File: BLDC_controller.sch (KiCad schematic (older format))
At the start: 97 parts, among them P1 CONN_01X02, P2 CONN_01X06, P3 CONN_01X05, P4 CONN_01X03, P5 CONN_01X05, Q1 PSMN2R0-30YLD, Q2 PSMN2R0-30YLD, Q3 PSMN2R0-30YLD, Q4 PSMN2R0-30YLD, Q5 PSMN2R0-30YLD, Q6 PSMN2R0-30YLD

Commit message: mostly routed
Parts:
- removed C20, C25, C26, C27: 220n, project_footprints:C_0805, symbol C
- C10, C11, C16, C22, C23, C24, C8, C9: footprint project_footprints:C_0402 -> project_footprints:C_0603
- C15, C21: value C -> 10p
- R1, R2, R3, R30, R31, R32, R33, R34, R35, R4, R40, R5, R6: footprint project_footprints:R_0603_NOM -> project_footprints:R_0603
- R10, R11, R12, R13, R14, R15, R16, R17, R18, R19, R20, R21, R22, R23, R24, R25, R26, R27, R28, R29, R36, R38, R39, R41, R42, R43, R44, R45, R46, R47: footprint project_footprints:R_0402_MOST -> project_footprints:R_0603
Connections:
- net GND: now also R14.1, R15.1, R16.1; no longer R14.2, R15.2, R16.2
- net OP4P: now reaches D1.1 (OP4P), R29.1
- net OP4N: now reaches D1.2 (OP4N), R47.2
- net OP1P: now reaches D1.23 (OP1P), R17.1, R20.2, R23.1
- net VBOOSTW: now reaches C3.2, D1.27 (VBOOTW)
- net VBOOSTV: now reaches C2.2, D1.31 (VBOOTV)
- net VBOOSTU: now reaches C1.2, D1.35 (VBOOTU)
- net OP2P: now reaches D1.41 (OP2P), R18.1, R21.2, R24.1
- net OP3P: now reaches D1.45 (OP3P), R19.1, R22.2, R25.1
- net U_SENSE_N renamed OP3N
- net OP3N: now also R15.2; no longer R15.1
- net V_SENSE_N renamed OP2N
- net OP2N: now also R16.2; no longer R16.1
- net W_SENSE_N renamed OP1N
- net OP1N: now also R14.2; no longer R14.1
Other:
- moved on the sheet: C1, C2, C3, R14, R15, R16

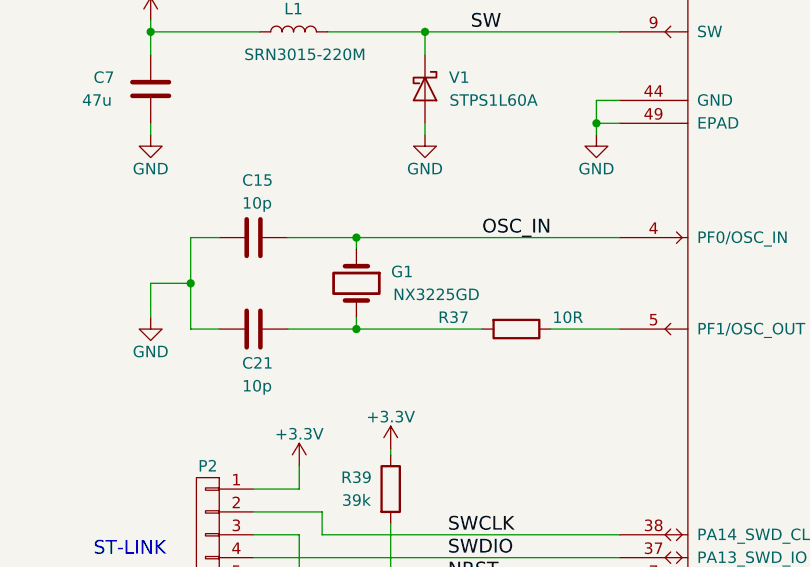
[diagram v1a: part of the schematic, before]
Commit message: keepouts added under sense resistors
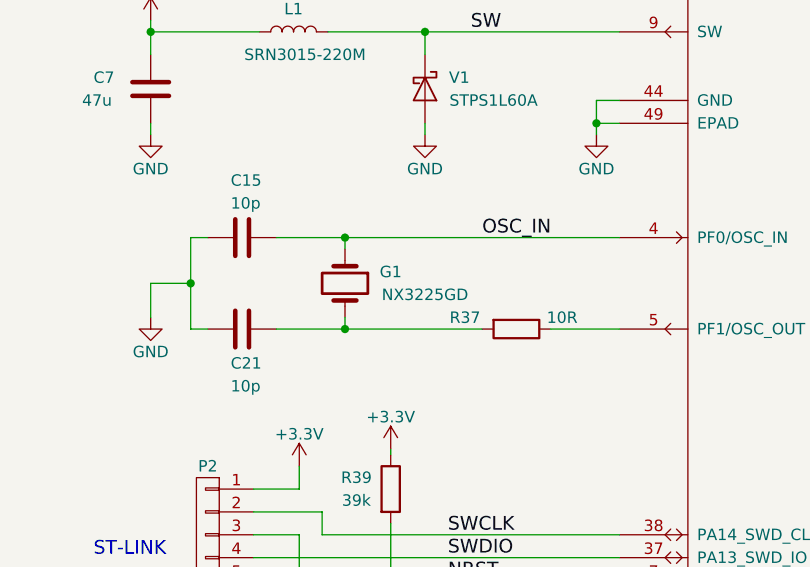
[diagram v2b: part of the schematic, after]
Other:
- moved on the sheet: C15, C21, G1
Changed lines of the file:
@@
 	6600 7900 7400 7900
-$Comp
-L R R37
-U 1 1 58A95F2B
-P 6950 3500
-F 0 "R37" V 6900 3225 50  0000 C CNN
-F 1 "10R" V 6900 3725 50  0000 C CNN
-F 2 "project_footprints:R_0402_MOST" V 6880 3500 50  0001 C CNN
-F 3 "" H 6950 3500 50  0000 C CNN
-	1    6950 3500
-	0    1    1    0
-$EndComp
 $Comp
 L GND #PWR051
@@
 $EndComp
 Wire Wire Line
-	6250 3150 6250 3100
-Wire Wire Line
-	5950 3100 7400 3100
-Wire Wire Line
-	6250 3450 6250 3500
+	6200 3150 6200 3100
+Wire Wire Line
+	5900 3100 7400 3100
+Wire Wire Line
+	6200 3450 6200 3500
 $Comp
 L C C15
 U 1 1 58AA5F93
-P 5800 3100
-F 0 "C15" V 5550 3050 50  0000 L CNN
-F 1 "10p" V 5650 3050 50  0000 L CNN
-F 2 "project_footprints:C_0402" H 5838 2950 50  0001 C CNN
-F 3 "" H 5800 3100 50  0000 C CNN
-	1    5800 3100
+P 5750 3100
+F 0 "C15" V 5500 3050 50  0000 L CNN
+F 1 "10p" V 5600 3050 50  0000 L CNN
+F 2 "project_footprints:C_0402" H 5788 2950 50  0001 C CNN
+F 3 "" H 5750 3100 50  0000 C CNN
+	1    5750 3100
 	0    1    1    0
 $EndComp
-Wire Wire Line
-	7100 3500 7400 3500
-Wire Wire Line
-	5950 3500 6800 3500
 $Comp
 L C C21
 U 1 1 58AA7DE1
-P 5800 3500
-F 0 "C21" V 5950 3450 50  0000 L CNN
-F 1 "10p" V 6050 3450 50  0000 L CNN
-F 2 "project_footprints:C_0402" H 5838 3350 50  0001 C CNN
-F 3 "" H 5800 3500 50  0000 C CNN
-	1    5800 3500
+P 5750 3500
+F 0 "C21" V 5900 3450 50  0000 L CNN
+F 1 "10p" V 6000 3450 50  0000 L CNN
+F 2 "project_footprints:C_0402" H 5788 3350 50  0001 C CNN
+F 3 "" H 5750 3500 50  0000 C CNN
+	1    5750 3500
 	0    1    1    0
 $EndComp
-Connection ~ 6250 3100
-Connection ~ 6250 3500
-Wire Wire Line
-	5525 3500 5650 3500
+Connection ~ 6200 3100
+Connection ~ 6200 3500
+Wire Wire Line
+	5525 3500 5600 3500
 Wire Wire Line
 	5525 3100 5525 3500
 Wire Wire Line
-	5525 3100 5650 3100
+	5525 3100 5600 3100
 Wire Wire Line
 	5350 3450 5350 3300
@@
 L Crystal G1
 U 1 1 58AD39C7
-P 6250 3300
-F 0 "G1" V 6200 3500 50  0000 C CNN
-F 1 "NX3225GD" V 6300 3650 50  0000 C CNN
-F 2 "project_footprints:Crystal_3225" H 6250 3300 50  0001 C CNN
-F 3 "" H 6250 3300 50  0000 C CNN
-	1    6250 3300
+P 6200 3300
+F 0 "G1" V 6150 3500 50  0000 C CNN
+F 1 "NX3225GD" V 6250 3650 50  0000 C CNN
+F 2 "project_footprints:Crystal_3225" H 6200 3300 50  0001 C CNN
+F 3 "" H 6200 3300 50  0000 C CNN
+	1    6200 3300
 	0    1    1    0
 $EndComp
@@
 Text Label 9400 6600 0    60   ~ 0
 VBOOSTW
+$Comp
+L R R37
+U 1 1 58B4856C
+P 6950 3500
+F 0 "R37" V 6900 3275 50  0000 C CNN
+F 1 "10R" V 6900 3700 50  0000 C CNN
+F 2 "project_footprints:R_0402_MOST" V 6880 3500 50  0001 C CNN
+F 3 "" H 6950 3500 50  0000 C CNN
+	1    6950 3500
+	0    1    1    0
+$EndComp
+Wire Wire Line
+	7100 3500 7400 3500
+Wire Wire Line
+	5900 3500 6800 3500
 $EndSCHEMATC

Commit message: Layout ready for 1st review
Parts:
- removed C18: 680u, project_footprints:C_Radial_D10_L25_P5, symbol CP
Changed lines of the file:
@@
-$EndComp
-$Comp
-L CP C18
-U 1 1 58A239DA
-P 4500 1400
-F 0 "C18" H 4200 1450 50  0000 L CNN
-F 1 "680u" H 4150 1350 50  0000 L CNN
-F 2 "project_footprints:C_Radial_D10_L25_P5" H 4538 1250 50  0001 C CNN
-F 3 "" H 4500 1400 50  0000 C CNN
-	1    4500 1400
-	1    0    0    -1
-$EndComp
-$Comp
-L GND #PWR039
-U 1 1 58A23D23
-P 4500 1600
-F 0 "#PWR039" H 4500 1350 50  0001 C CNN
-F 1 "GND" H 4500 1450 50  0000 C CNN
-F 2 "" H 4500 1600 50  0000 C CNN
-F 3 "" H 4500 1600 50  0000 C CNN
-	1    4500 1600
-	1    0    0    -1
 $EndComp
 $Comp
@@
 	2000 1200 1900 1200
 Wire Wire Line
-	4500 1550 4500 1600
-Wire Wire Line
-	4500 1100 4500 1250
-Connection ~ 4500 1100
-Wire Wire Line
 	3100 2400 3100 2300

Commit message: minor improvements
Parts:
- added R48: 560R, project_footprints:R_0603, symbol R
- added V8: LED_ALT, project_footprints:LED_0402, symbol LED_ALT
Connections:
- net GND: now also V8.1 (K)
- net PA2: now reaches D1.13 (PA2/ADC_IN2)
- net PA2: now also R48.1
- new net PA2_LED: R48.2, V8.2 (A)
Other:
- moved on the sheet: C22, C23, C24, P5, R41, R42, R43, R44, R45, R46

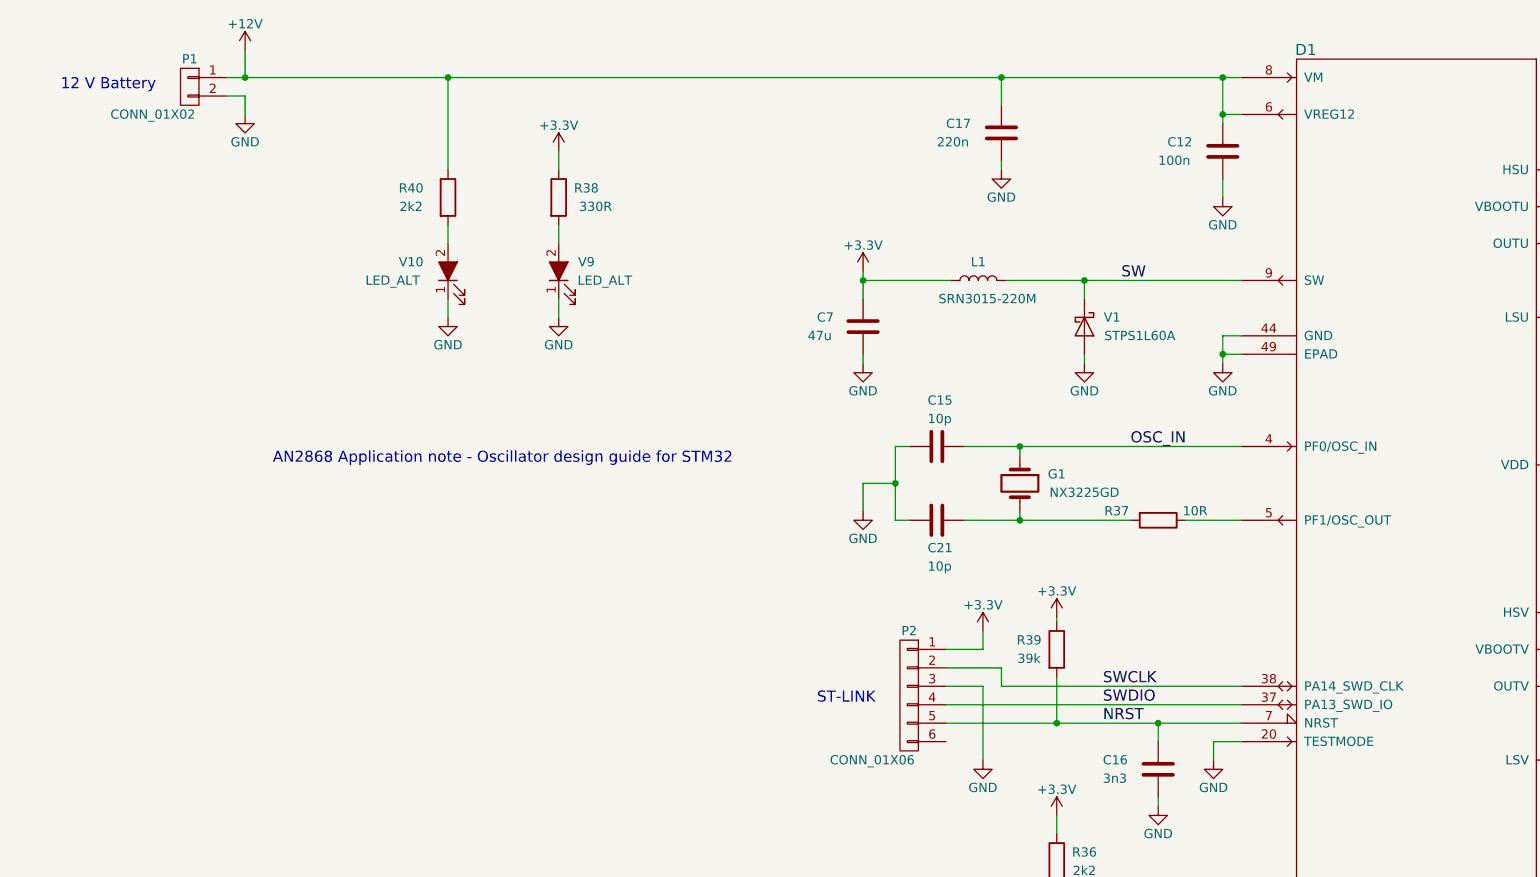
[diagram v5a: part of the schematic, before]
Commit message: Add Helsinki Hacklab logo
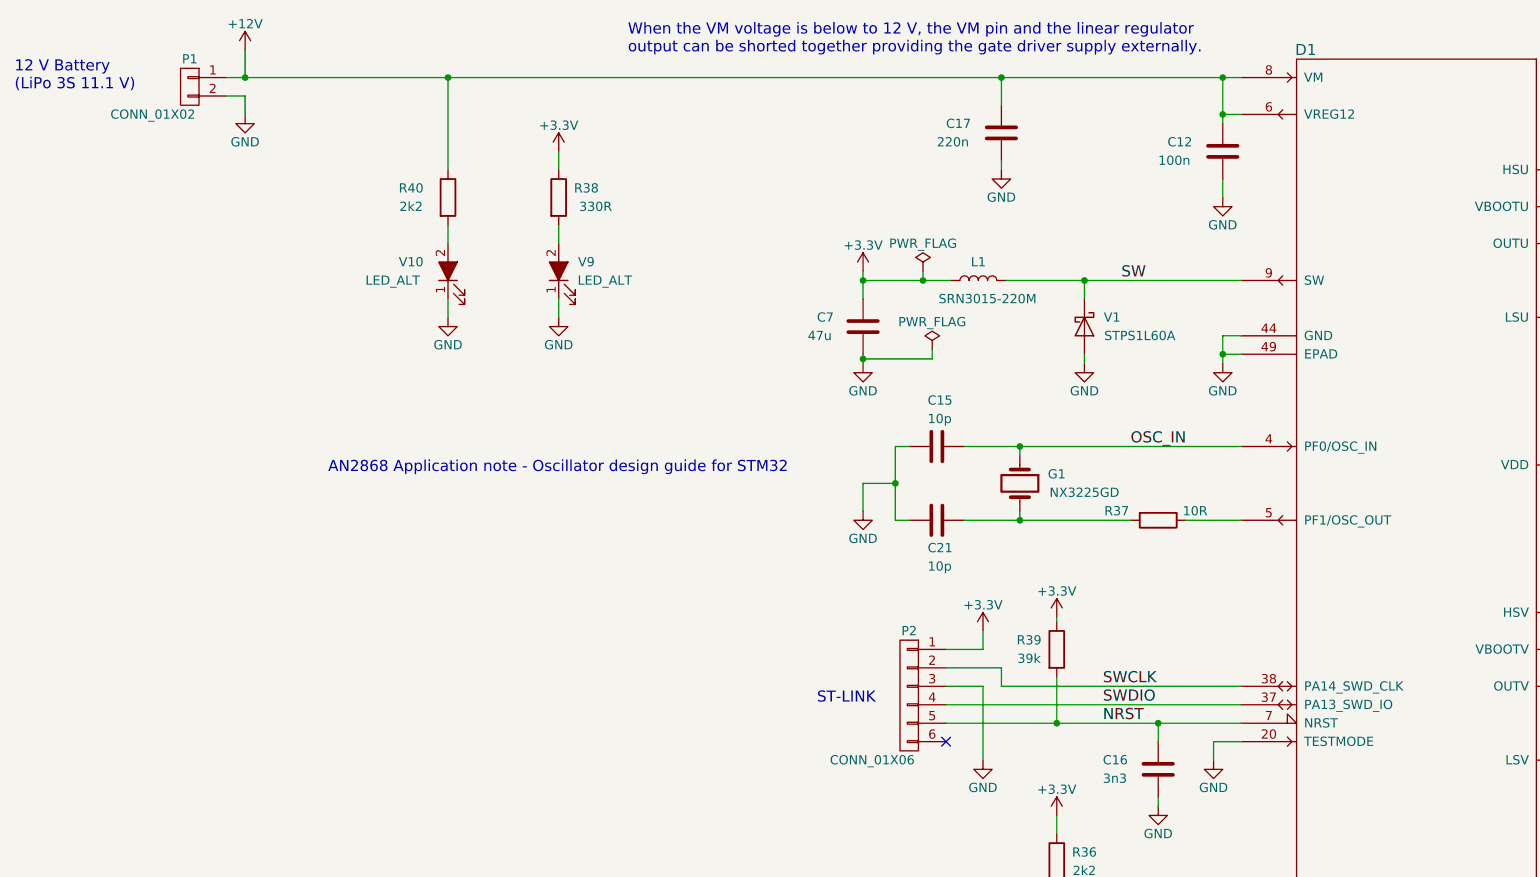
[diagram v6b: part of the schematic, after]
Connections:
- no-connect marks 0 -> 1
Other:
- note added: "12 V Battery\n(LiPo 3S 11.1 V)"
- note added: "When the VM voltage is below to 12 V, the VM pin and the linear regulator \noutput can be shorted together providing the gate driver supply externally."
- note removed: "12 V Battery"
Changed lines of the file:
@@
 Sheet 1 1
 Title "BLDC CONTROLLER"
-Date "07.03.2017"
+Date "22.3.2017"
 Rev "1.0"
 Comp "Helsinki Hacklab"
@@
 	5350 2650 5350 2600
 Wire Wire Line
-	5825 2200 5350 2200
+	5350 2200 5825 2200
 Wire Wire Line
 	5350 2150 5350 2300
@@
 Text Notes 4900 5825 0    60   ~ 0
 SPI interface
-Text Notes 1000 1175 0    60   ~ 0
-12 V Battery
+Text Notes 750  1175 0    60   ~ 0
+12 V Battery\n(LiPo 3S 11.1 V)
 Text Notes 15450 4550 0    60   ~ 0
 BLDC motor
@@
 Text Notes 12300 8450 0    60   ~ 0
 15 A current through a sense resistor causes 2.25 W heat dissipation. \nHowever, none of the three sense resistor conducts 100% of the time.
-Text Notes 2150 3200 0    60   ~ 0
+Text Notes 2450 3250 0    60   ~ 0
 AN2868 Application note - Oscillator design guide for STM32
 Text Label 6800 3100 0    60   ~ 0
@@
 Text Label 7200 6900 0    60   ~ 0
 PA2
+NoConn ~ 5800 4700
+$Comp
+L PWR_FLAG #FLG059
+U 1 1 58D32B00
+P 5675 2150
+F 0 "#FLG059" H 5675 2225 50  0001 C CNN
+F 1 "PWR_FLAG" H 5675 2300 50  0000 C CNN
+F 2 "" H 5675 2150 50  0001 C CNN
+F 3 "" H 5675 2150 50  0001 C CNN
+	1    5675 2150
+	1    0    0    -1
+$EndComp
+Wire Wire Line
+	5675 2150 5675 2200
+Connection ~ 5675 2200
+$Comp
+L PWR_FLAG #FLG060
+U 1 1 58D33188
+P 5725 2575
+F 0 "#FLG060" H 5725 2650 50  0001 C CNN
+F 1 "PWR_FLAG" H 5725 2725 50  0000 C CNN
+F 2 "" H 5725 2575 50  0001 C CNN
+F 3 "" H 5725 2575 50  0001 C CNN
+	1    5725 2575
+	1    0    0    -1
+$EndComp
+Wire Wire Line
+	5725 2575 5725 2625
+Wire Wire Line
+	5725 2625 5350 2625
+Connection ~ 5350 2625
+Text Notes 4075 975  0    60   ~ 0
+When the VM voltage is below to 12 V, the VM pin and the linear regulator \noutput can be shorted together providing the gate driver supply externally.
 $EndSCHEMATC
